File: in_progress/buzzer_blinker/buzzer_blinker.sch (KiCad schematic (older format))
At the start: 12 parts, among them SW1 SW_PUSH, SW2 SWITCH_INV

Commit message: .
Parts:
- removed SW2: SWITCH_INV, symbol SWITCH_INV
- added F1: FUSE, 250 mA, symbol FUSE
- added R1: R, 10M 1/4W, symbol R
- added SW2: SWITCH_DPDT, symbol SWITCH_DPDT
- renumbered R1 to R2
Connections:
- net LIVE: now also SW2.5
- net NEUTRAL: now also SW2.1
- net at C1.1, D1.2 (A), D2.1 (K): now also R1.1
- net at C1.2: now also F1.2, R1.2
- net at SP1.1: now also SW2.2
- new net: F1.1, SW2.6
- no-connect marks 0 -> 2
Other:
- moved on the sheet: C1, C2, D1, D2, D3, D4, D5, D6, R2, SP1, SW1

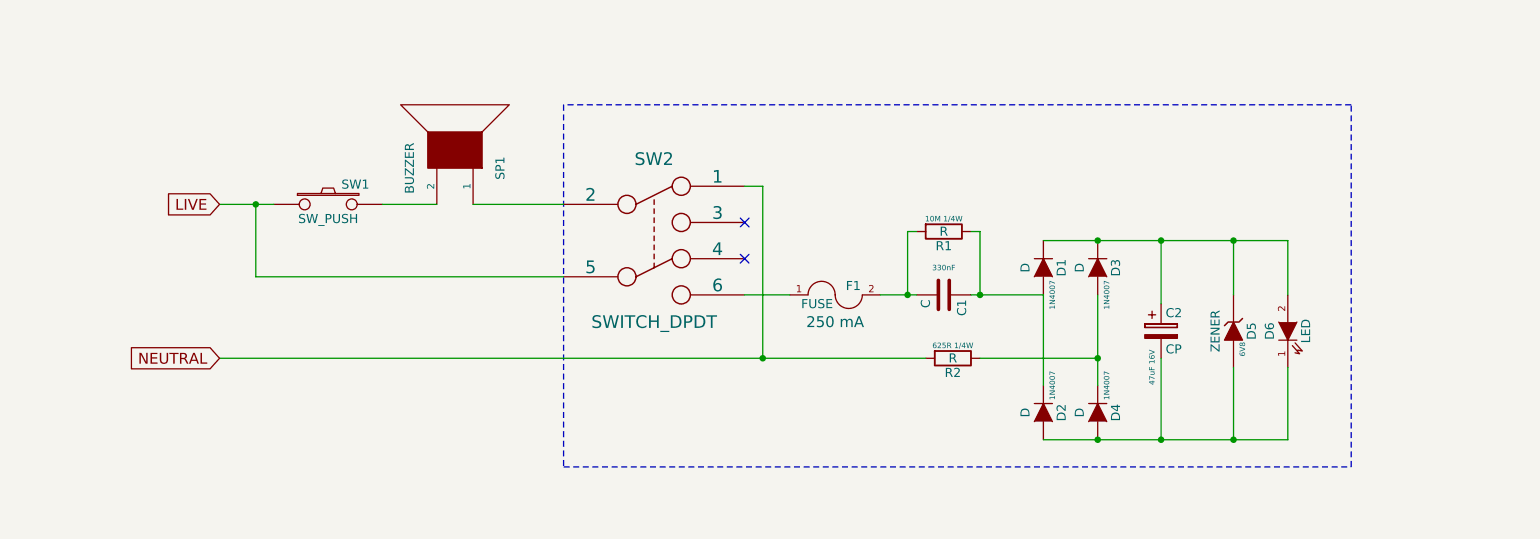
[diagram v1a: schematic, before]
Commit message: Changing the buzzer layout
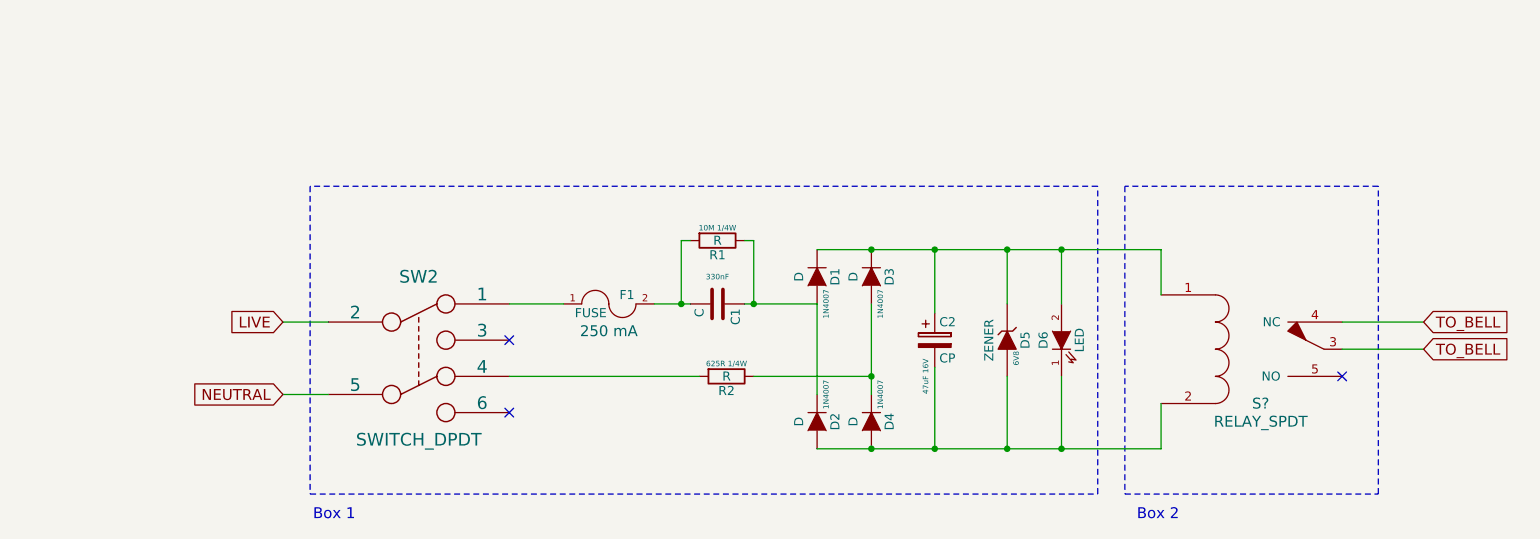
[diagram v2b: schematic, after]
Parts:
- removed SP1: BUZZER, symbol SPEAKER
- removed SW1: SW_PUSH, symbol SW_PUSH
- added S?: RELAY_SPDT, symbol RELAY_SPDT
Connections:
- net LIVE: now also SW2.2; no longer SW2.5
- net NEUTRAL: now also SW2.5; no longer R2.2, SW2.1
- net at C2.1, D1.1 (K), D3.1 (K)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: now also S?.1
- net at C2.2, D2.2 (A), D4.2 (A)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: now also S?.2
- net at SW2.4: now also R2.2
- net at F1.1: now also SW2.1; no longer SW2.6
- new net TO_BELL: S?.3, S?.4 (NC)
- no-connect marks 2 -> 3
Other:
- note added: "Box 1"
- note added: "Box 2"
- moved on the sheet: C1, C2, D1, D2, D3, D4, D5, D6, F1, R1, R2, SW2
